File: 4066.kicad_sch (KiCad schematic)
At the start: 1 part, among them U5 CD4066BE

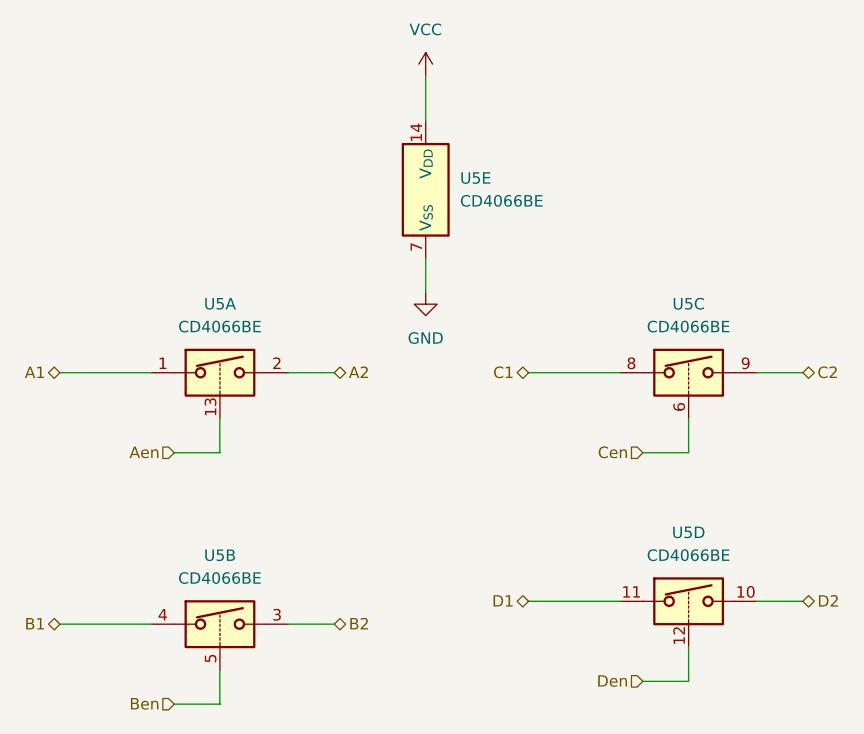
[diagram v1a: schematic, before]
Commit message: schematic doubling without pcb placing
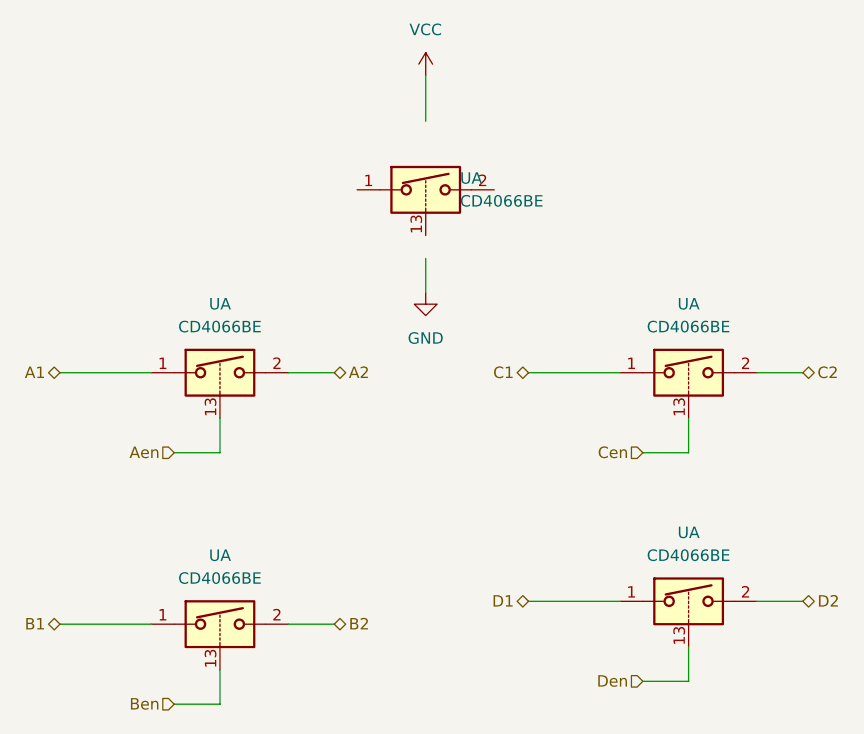
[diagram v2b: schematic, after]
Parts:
- renumbered U5 to U
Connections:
- net B1: now also U.1; no longer U.4
- net B2: now also U.2; no longer U.3
- net Ben: now also U.13; no longer U.5
- net C1: now also U.1; no longer U.8
- net C2: now also U.2; no longer U.9
- net Cen: now also U.13; no longer U.6
- net D1: now also U.1; no longer U.11
- net D2: now also U.2; no longer U.10
- net Den: now also U.13; no longer U.12
- net GND: no longer U.7 (V_{SS})
- net VCC: no longer U.14 (V_{DD})
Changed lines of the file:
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@@
 		(dnp no)
 		(fields_autoplaced yes)
-		(property "Reference" "#PWR054"
+		(property "Reference" "#PWR"
 			(at 120.65 50.8 0)
 			(effects
@@
 		(pin "1"
 		)
-		(instances
-			(project ""
-				(path "/01c1f2c1-4d06-4880-847a-9ab55552e3fd/22f83b5a-3e98-4c49-ae4d-8756987d640f"
-					(reference "#PWR054")
-					(unit 1)
-				)
-			)
-		)
+		(instances)
 	)
 	(symbol
 		(lib_id "Analog_Switch:CD4066BE")
 		(at 120.65 33.02 0)
-		(unit 5)
+		(unit 1)
 		(exclude_from_sim no)
 		(in_bom yes)
@@
 		(dnp no)
 		(fields_autoplaced yes)
-		(property "Reference" "U5"
+		(property "Reference" "U"
 			(at 124.46 31.7499 0)
 			(effects
@@
 		(pin "6"
 		)
-		(instances
-			(project ""
-				(path "/01c1f2c1-4d06-4880-847a-9ab55552e3fd/22f83b5a-3e98-4c49-ae4d-8756987d640f"
-					(reference "U5")
-					(unit 5)
-				)
-			)
-		)
+		(instances)
 	)
 	(symbol
@@
 		(dnp no)
 		(fields_autoplaced yes)
-		(property "Reference" "U5"
+		(property "Reference" "U"
 			(at 97.79 45.72 0)
 			(effects
@@
 		(pin "6"
 		)
-		(instances
-			(project ""
-				(path "/01c1f2c1-4d06-4880-847a-9ab55552e3fd/22f83b5a-3e98-4c49-ae4d-8756987d640f"
-					(reference "U5")
-					(unit 1)
-				)
-			)
-		)
+		(instances)
 	)
 	(symbol
@@
 		(dnp no)
 		(fields_autoplaced yes)
-		(property "Reference" "#PWR053"
+		(property "Reference" "#PWR"
 			(at 120.65 24.13 0)
 			(effects
@@
 		(pin "1"
 		)
-		(instances
-			(project ""
-				(path "/01c1f2c1-4d06-4880-847a-9ab55552e3fd/22f83b5a-3e98-4c49-ae4d-8756987d640f"
-					(reference "#PWR053")
-					(unit 1)
-				)
-			)
-		)
+		(instances)
 	)
 	(symbol
 		(lib_id "Analog_Switch:CD4066BE")
 		(at 97.79 81.28 0)
-		(unit 2)
+		(unit 1)
 		(exclude_from_sim no)
 		(in_bom yes)
@@
 		(dnp no)
 		(fields_autoplaced yes)
-		(property "Reference" "U5"
+		(property "Reference" "U"
 			(at 97.79 73.66 0)
 			(effects
@@
 		(pin "6"
 		)
-		(instances
-			(project ""
-				(path "/01c1f2c1-4d06-4880-847a-9ab55552e3fd/22f83b5a-3e98-4c49-ae4d-8756987d640f"
-					(reference "U5")
-					(unit 2)
-				)
-			)
-		)
+		(instances)
 	)
 	(symbol
 		(lib_id "Analog_Switch:CD4066BE")
 		(at 149.86 53.34 0)
-		(unit 3)
+		(unit 1)
 		(exclude_from_sim no)
 		(in_bom yes)
@@
 		(dnp no)
 		(fields_autoplaced yes)
-		(property "Reference" "U5"
+		(property "Reference" "U"
 			(at 149.86 45.72 0)
 			(effects
@@
 		(pin "6"
 		)
-		(instances
-			(project ""
-				(path "/01c1f2c1-4d06-4880-847a-9ab55552e3fd/22f83b5a-3e98-4c49-ae4d-8756987d640f"
-					(reference "U5")
-					(unit 3)
-				)
-			)
-		)
+		(instances)
 	)
 	(symbol
 		(lib_id "Analog_Switch:CD4066BE")
 		(at 149.86 78.74 0)
-		(unit 4)
+		(unit 1)
 		(exclude_from_sim no)
 		(in_bom yes)
@@
 		(dnp no)
 		(fields_autoplaced yes)
-		(property "Reference" "U5"
+		(property "Reference" "U"
 			(at 149.86 71.12 0)
 			(effects
@@
 		(pin "6"
 		)
-		(instances
-			(project ""
-				(path "/01c1f2c1-4d06-4880-847a-9ab55552e3fd/22f83b5a-3e98-4c49-ae4d-8756987d640f"
-					(reference "U5")
-					(unit 4)
-				)
-			)
-		)
+		(instances)
 	)
 )

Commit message: pcb placing doubling without routing
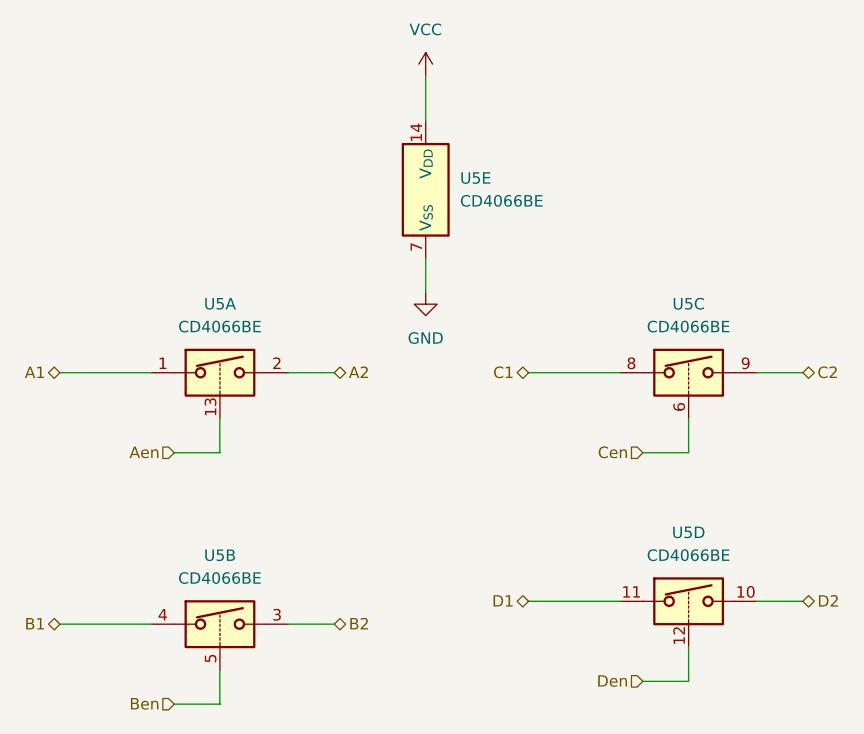
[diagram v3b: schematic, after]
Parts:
- removed U (x5): CD4066BE, Package_DIP:DIP-14_W7.62mm, symbol Analog_Switch:CD4066BE
- added U5: CD4066BE, Package_DIP:DIP-14_W7.62mm, symbol Analog_Switch:CD4066BE
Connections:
- net A1: now also U5.1
- net A2: now also U5.2
- net Aen: now also U5.13
- net B1: now also U5.4
- net B2: now also U5.3
- net Ben: now also U5.5
- net C1: now also U5.8
- net C2: now also U5.9
- net Cen: now also U5.6
- net D1: now also U5.11
- net D2: now also U5.10
- net Den: now also U5.12
- net GND: now also U5.7 (V_{SS})
- net VCC: now also U5.14 (V_{DD})

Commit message: v2 initial commit
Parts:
- renumbered U5 to U9
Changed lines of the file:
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@@
 		(dnp no)
 		(fields_autoplaced yes)
-		(property "Reference" "#PWR0107"
+		(property "Reference" "#PWR043"
 			(at 120.65 50.8 0)
 			(effects
@@
 		(instances
 			(project "kleingorium"
-				(path "/01c1f2c1-4d06-4880-847a-9ab55552e3fd/22f83b5a-3e98-4c49-ae4d-8756987d640f"
-					(reference "#PWR0107")
+				(path "/01c1f2c1-4d06-4880-847a-9ab55552e3fd/ad1f1d92-237d-4bc3-883c-2ce266dd223f/7cea744f-aacf-435a-ae2b-eca174bccc85"
+					(reference "#PWR043")
 					(unit 1)
 				)
@@
 		(dnp no)
 		(fields_autoplaced yes)
-		(property "Reference" "U5"
+		(property "Reference" "U9"
 			(at 149.86 45.72 0)
 			(effects
@@
 		)
 		(instances
-			(project ""
-				(path "/01c1f2c1-4d06-4880-847a-9ab55552e3fd/22f83b5a-3e98-4c49-ae4d-8756987d640f"
-					(reference "U5")
+			(project "kleingorium"
+				(path "/01c1f2c1-4d06-4880-847a-9ab55552e3fd/ad1f1d92-237d-4bc3-883c-2ce266dd223f/7cea744f-aacf-435a-ae2b-eca174bccc85"
+					(reference "U9")
 					(unit 3)
 				)
@@
 		(dnp no)
 		(fields_autoplaced yes)
-		(property "Reference" "U5"
+		(property "Reference" "U9"
 			(at 97.79 45.72 0)
 			(effects
@@
 		)
 		(instances
-			(project ""
-				(path "/01c1f2c1-4d06-4880-847a-9ab55552e3fd/22f83b5a-3e98-4c49-ae4d-8756987d640f"
-					(reference "U5")
+			(project "kleingorium"
+				(path "/01c1f2c1-4d06-4880-847a-9ab55552e3fd/ad1f1d92-237d-4bc3-883c-2ce266dd223f/7cea744f-aacf-435a-ae2b-eca174bccc85"
+					(reference "U9")
 					(unit 1)
 				)
@@
 		(dnp no)
 		(fields_autoplaced yes)
-		(property "Reference" "U5"
+		(property "Reference" "U9"
 			(at 97.79 73.66 0)
 			(effects
@@
 		)
 		(instances
-			(project ""
-				(path "/01c1f2c1-4d06-4880-847a-9ab55552e3fd/22f83b5a-3e98-4c49-ae4d-8756987d640f"
-					(reference "U5")
+			(project "kleingorium"
+				(path "/01c1f2c1-4d06-4880-847a-9ab55552e3fd/ad1f1d92-237d-4bc3-883c-2ce266dd223f/7cea744f-aacf-435a-ae2b-eca174bccc85"
+					(reference "U9")
 					(unit 2)
 				)
@@
 		(dnp no)
 		(fields_autoplaced yes)
-		(property "Reference" "#PWR0108"
+		(property "Reference" "#PWR042"
 			(at 120.65 24.13 0)
 			(effects
@@
 		(instances
 			(project "kleingorium"
-				(path "/01c1f2c1-4d06-4880-847a-9ab55552e3fd/22f83b5a-3e98-4c49-ae4d-8756987d640f"
-					(reference "#PWR0108")
+				(path "/01c1f2c1-4d06-4880-847a-9ab55552e3fd/ad1f1d92-237d-4bc3-883c-2ce266dd223f/7cea744f-aacf-435a-ae2b-eca174bccc85"
+					(reference "#PWR042")
 					(unit 1)
 				)
@@
 		(dnp no)
 		(fields_autoplaced yes)
-		(property "Reference" "U5"
+		(property "Reference" "U9"
 			(at 124.46 31.7499 0)
 			(effects
@@
 		)
 		(instances
-			(project ""
-				(path "/01c1f2c1-4d06-4880-847a-9ab55552e3fd/22f83b5a-3e98-4c49-ae4d-8756987d640f"
-					(reference "U5")
+			(project "kleingorium"
+				(path "/01c1f2c1-4d06-4880-847a-9ab55552e3fd/ad1f1d92-237d-4bc3-883c-2ce266dd223f/7cea744f-aacf-435a-ae2b-eca174bccc85"
+					(reference "U9")
 					(unit 5)
 				)
@@
 		(dnp no)
 		(fields_autoplaced yes)
-		(property "Reference" "U5"
+		(property "Reference" "U9"
 			(at 149.86 71.12 0)
 			(effects
@@
 		)
 		(instances
-			(project ""
-				(path "/01c1f2c1-4d06-4880-847a-9ab55552e3fd/22f83b5a-3e98-4c49-ae4d-8756987d640f"
-					(reference "U5")
+			(project "kleingorium"
+				(path "/01c1f2c1-4d06-4880-847a-9ab55552e3fd/ad1f1d92-237d-4bc3-883c-2ce266dd223f/7cea744f-aacf-435a-ae2b-eca174bccc85"
+					(reference "U9")
 					(unit 4)
 				)
